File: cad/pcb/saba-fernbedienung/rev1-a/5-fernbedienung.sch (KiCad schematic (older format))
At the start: 49 parts, among them K601 G6K-2, K602 G6K-2, K603 G6K-2, K604 G6K-2, K605 G6K-2, K606 G6K-2, K607 EC2-5TNU, Q601 BC846, Q602 BC846, Q603 BC846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

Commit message: Fix: Div. DRC
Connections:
- no-connect marks 6 -> 12
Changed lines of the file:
@@
 Text Notes 4100 5150 0    79   ~ 0
 Netzschalter
+NoConn ~ 7650 2800
+NoConn ~ 7850 2800
+NoConn ~ 7650 4200
+NoConn ~ 7850 4200
+NoConn ~ 7650 1200
+NoConn ~ 7850 1200
 $EndSCHEMATC

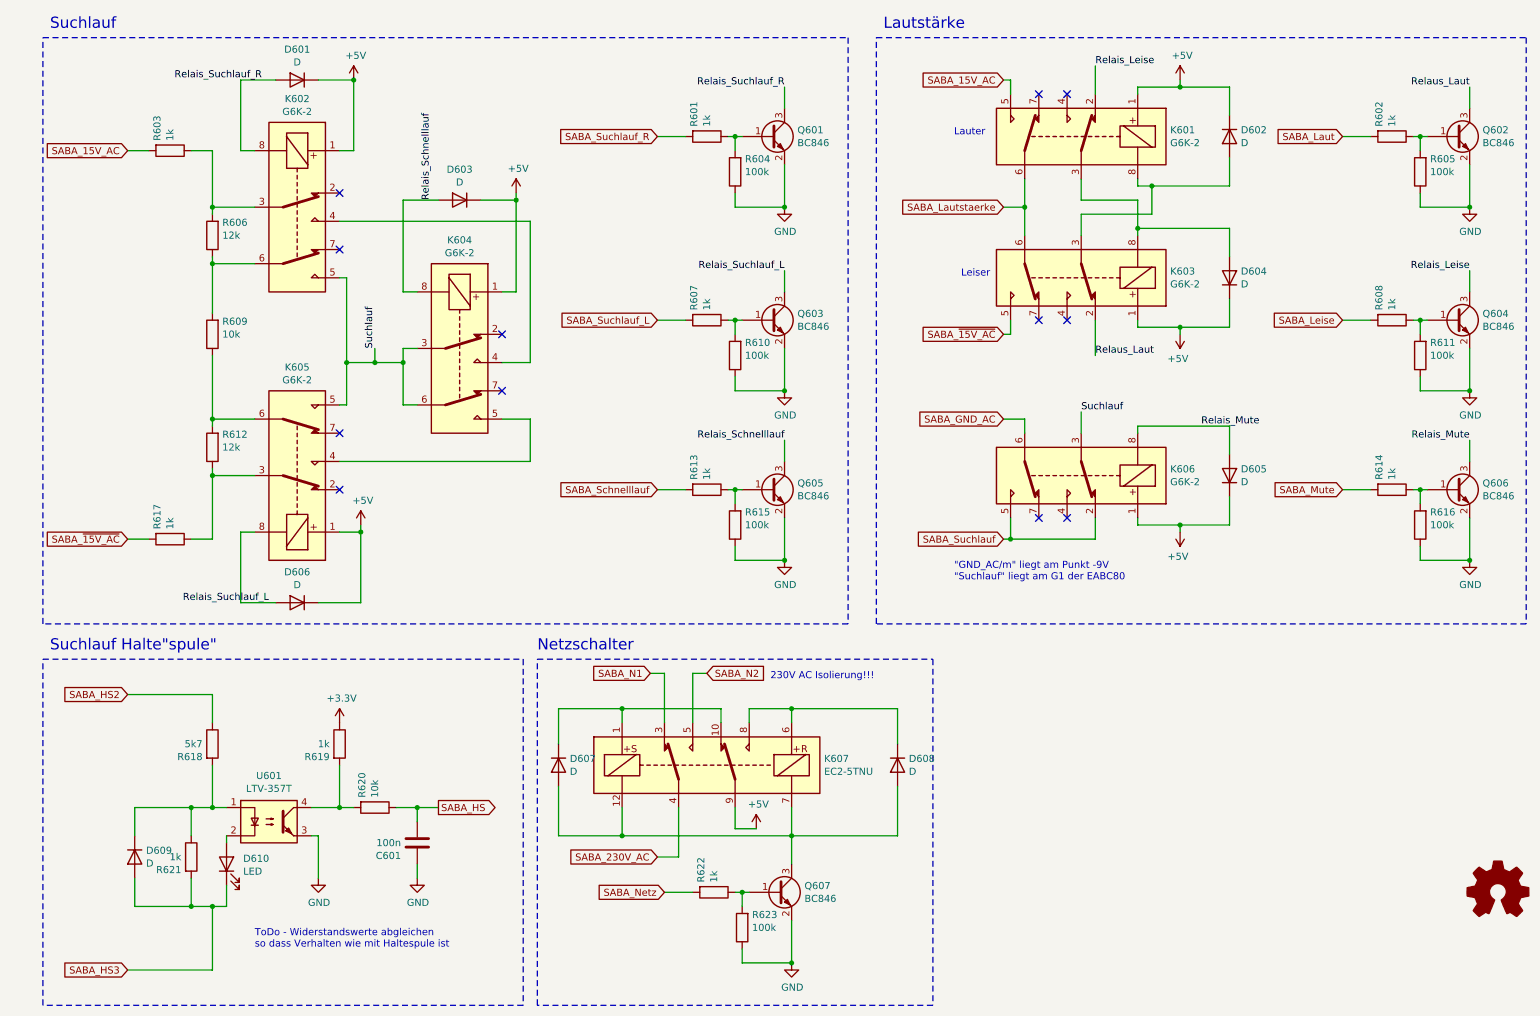
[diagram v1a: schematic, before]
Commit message: New: Bauteil - Pad Zuordnungen
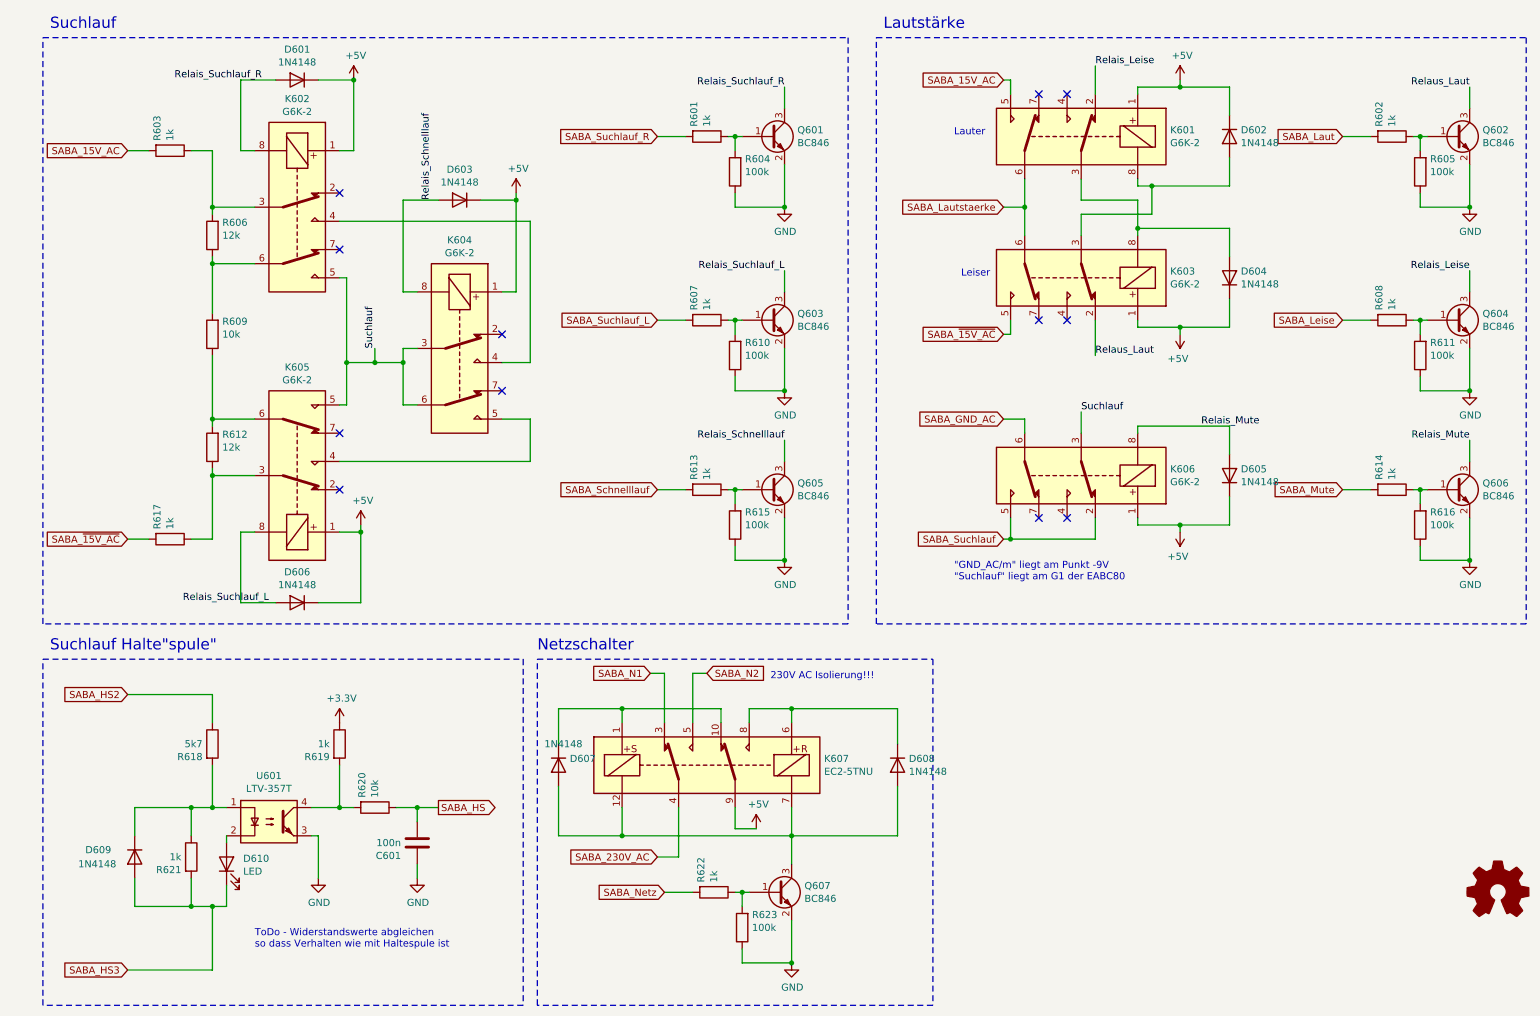
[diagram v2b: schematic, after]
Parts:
- D601, D602, D603, D604, D605, D606, D607, D608, D609: value D -> 1N4148; footprint (none) -> Diode_SMD:D_SOD-323F
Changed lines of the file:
@@
-$EndComp
-$Comp
-L Relay:G6K-2 K604
-U 1 1 60038514
-P 3550 3000
-F 0 "K604" V 2783 3000 50  0000 C CNN
-F 1 "G6K-2" V 2874 3000 50  0000 C CNN
-F 2 "Relay_SMD:Relay_DPDT_Omron_G6K-2F" H 3550 3000 50  0001 L CNN
-F 3 "http://omronfs.omron.com/en_US/ecb/products/pdf/en-g6k.pdf" H 3550 3000 50  0001 C CNN
-	1    3550 3000
-	0    1    1    0
 $EndComp
 $Comp
@@
 P 2400 4800
 F 0 "D606" H 2400 5017 50  0000 C CNN
-F 1 "D" H 2400 4926 50  0000 C CNN
-F 2 "" H 2400 4800 50  0001 C CNN
+F 1 "1N4148" H 2400 4926 50  0000 C CNN
+F 2 "Diode_SMD:D_SOD-323F" H 2400 4800 50  0001 C CNN
 F 3 "~" H 2400 4800 50  0001 C CNN
 	1    2400 4800
@@
 P 3550 1950
 F 0 "D603" H 3550 2167 50  0000 C CNN
-F 1 "D" H 3550 2076 50  0000 C CNN
-F 2 "" H 3550 1950 50  0001 C CNN
+F 1 "1N4148" H 3550 2076 50  0000 C CNN
+F 2 "Diode_SMD:D_SOD-323F" H 3550 1950 50  0001 C CNN
 F 3 "~" H 3550 1950 50  0001 C CNN
 	1    3550 1950
@@
 P 2400 1100
 F 0 "D601" H 2400 1317 50  0000 C CNN
-F 1 "D" H 2400 1226 50  0000 C CNN
-F 2 "" H 2400 1100 50  0001 C CNN
+F 1 "1N4148" H 2400 1226 50  0000 C CNN
+F 2 "Diode_SMD:D_SOD-323F" H 2400 1100 50  0001 C CNN
 F 3 "~" H 2400 1100 50  0001 C CNN
 	1    2400 1100
@@
 Connection ~ 2750 3100
 Wire Wire Line
-	3150 3400 3150 3100
-Wire Wire Line
 	2750 3100 2750 3400
-Wire Wire Line
-	3950 2600 3950 1950
 Wire Wire Line
 	3150 1950 3400 1950
@@
 Relais_Suchlauf_L
 Wire Wire Line
-	3250 3400 3150 3400
-Wire Wire Line
-	3250 3000 3150 3000
-Wire Wire Line
-	3150 3000 3150 3100
-Connection ~ 3150 3100
-Wire Wire Line
-	4050 3100 3850 3100
-Wire Wire Line
 	4050 2100 4050 3100
-Wire Wire Line
-	4050 3500 3850 3500
-Wire Wire Line
-	3950 2600 3850 2600
-Wire Wire Line
-	3250 2600 3150 2600
 Text GLabel 4950 4000 0    50   Input ~ 0
 SABA_Schnelllauf
@@
 	1    0    0    -1
 $EndComp
-Wire Wire Line
-	3150 1950 3150 2600
 Wire Wire Line
 	2000 1100 2000 1600
@@
 U 1 1 6014EEE0
 P 1250 6600
-F 0 "D609" V 1204 6520 50  0000 R CNN
-F 1 "D" V 1295 6520 50  0000 R CNN
-F 2 "" H 1250 6600 50  0001 C CNN
+F 0 "D609" V 1200 6950 50  0000 R CNN
+F 1 "1N4148" V 1300 7000 50  0000 R CNN
+F 2 "Diode_SMD:D_SOD-323F" H 1250 6600 50  0001 C CNN
 F 3 "~" H 1250 6600 50  0001 C CNN
 	1    1250 6600
@@
 NoConn ~ 2700 1900
 NoConn ~ 2700 2300
-NoConn ~ 3850 2900
-NoConn ~ 3850 3300
 NoConn ~ 2700 3600
 NoConn ~ 2700 4000
@@
 P 9000 1500
 F 0 "D602" V 8954 1420 50  0000 R CNN
-F 1 "D" V 9045 1420 50  0000 R CNN
-F 2 "" H 9000 1500 50  0001 C CNN
+F 1 "1N4148" V 9045 1420 50  0000 R CNN
+F 2 "Diode_SMD:D_SOD-323F" H 9000 1500 50  0001 C CNN
 F 3 "~" H 9000 1500 50  0001 C CNN
 	1    9000 1500
@@
 P 9000 2500
 F 0 "D604" V 9046 2580 50  0000 L CNN
-F 1 "D" V 8955 2580 50  0000 L CNN
-F 2 "" H 9000 2500 50  0001 C CNN
+F 1 "1N4148" V 8955 2580 50  0000 L CNN
+F 2 "Diode_SMD:D_SOD-323F" H 9000 2500 50  0001 C CNN
 F 3 "~" H 9000 2500 50  0001 C CNN
 	1    9000 2500
@@
 P 9000 3900
 F 0 "D605" V 9046 3980 50  0000 L CNN
-F 1 "D" V 8955 3980 50  0000 L CNN
-F 2 "" H 9000 3900 50  0001 C CNN
+F 1 "1N4148" V 8955 3980 50  0000 L CNN
+F 2 "Diode_SMD:D_SOD-323F" H 9000 3900 50  0001 C CNN
 F 3 "~" H 9000 3900 50  0001 C CNN
 	1    9000 3900
@@
 	2950 3000 2950 3100
 Connection ~ 2950 3100
-Wire Wire Line
-	2950 3100 3150 3100
 Text Label 7950 3450 0    50   ~ 0
 Suchlauf
@@
 P 4250 5950
 F 0 "D607" V 4204 5870 50  0000 R CNN
-F 1 "D" V 4295 5870 50  0000 R CNN
-F 2 "" H 4250 5950 50  0001 C CNN
+F 1 "1N4148" V 4100 6050 50  0000 R CNN
+F 2 "Diode_SMD:D_SOD-323F" H 4250 5950 50  0001 C CNN
 F 3 "~" H 4250 5950 50  0001 C CNN
 	1    4250 5950
@@
 P 6650 5950
 F 0 "D608" V 6604 5870 50  0000 R CNN
-F 1 "D" V 6695 5870 50  0000 R CNN
-F 2 "" H 6650 5950 50  0001 C CNN
+F 1 "1N4148" V 6695 5870 50  0000 R CNN
+F 2 "Diode_SMD:D_SOD-323F" H 6650 5950 50  0001 C CNN
 F 3 "~" H 6650 5950 50  0001 C CNN
 	1    6650 5950
@@
 NoConn ~ 7650 1200
 NoConn ~ 7850 1200
+Wire Wire Line
+	2950 3100 3150 3100
+NoConn ~ 3850 3300
+NoConn ~ 3850 2900
+Wire Wire Line
+	3150 1950 3150 2600
+Wire Wire Line
+	3250 2600 3150 2600
+Wire Wire Line
+	3950 2600 3850 2600
+Wire Wire Line
+	4050 3500 3850 3500
+Wire Wire Line
+	4050 3100 3850 3100
+Connection ~ 3150 3100
+Wire Wire Line
+	3150 3000 3150 3100
+Wire Wire Line
+	3250 3000 3150 3000
+Wire Wire Line
+	3250 3400 3150 3400
+Wire Wire Line
+	3950 2600 3950 1950
+Wire Wire Line
+	3150 3400 3150 3100
+$Comp
+L Relay:G6K-2 K604
+U 1 1 60038514
+P 3550 3000
+F 0 "K604" V 2783 3000 50  0000 C CNN
+F 1 "G6K-2" V 2874 3000 50  0000 C CNN
+F 2 "Relay_SMD:Relay_DPDT_Omron_G6K-2F" H 3550 3000 50  0001 L CNN
+F 3 "http://omronfs.omron.com/en_US/ecb/products/pdf/en-g6k.pdf" H 3550 3000 50  0001 C CNN
+	1    3550 3000
+	0    1    1    0
+$EndComp
 $EndSCHEMATC

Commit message: Add: Bauteiltypen Digikey...
viele Bauteile von WE da hoffentlich lange gueltig...
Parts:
- C601: Bauteil (none) -> WE 885382206004
- D601, D602, D603, D604, D605, D606, D607, D608, D609: Bauteil (none) -> ON 1N4148WS
- D610: Bauteil (none) -> WE 150080BS75000
- K601, K602, K603, K604, K605, K606: Bauteil (none) -> Omron G6K-2F-TR DC5
- K607: Bauteil (none) -> Kemet EC2-5TNU
- Q601, Q602, Q603, Q604, Q605, Q606, Q607: Bauteil (none) -> ON BC846BLT3G
- U601: Bauteil (none) -> Lite-On LTV-357T

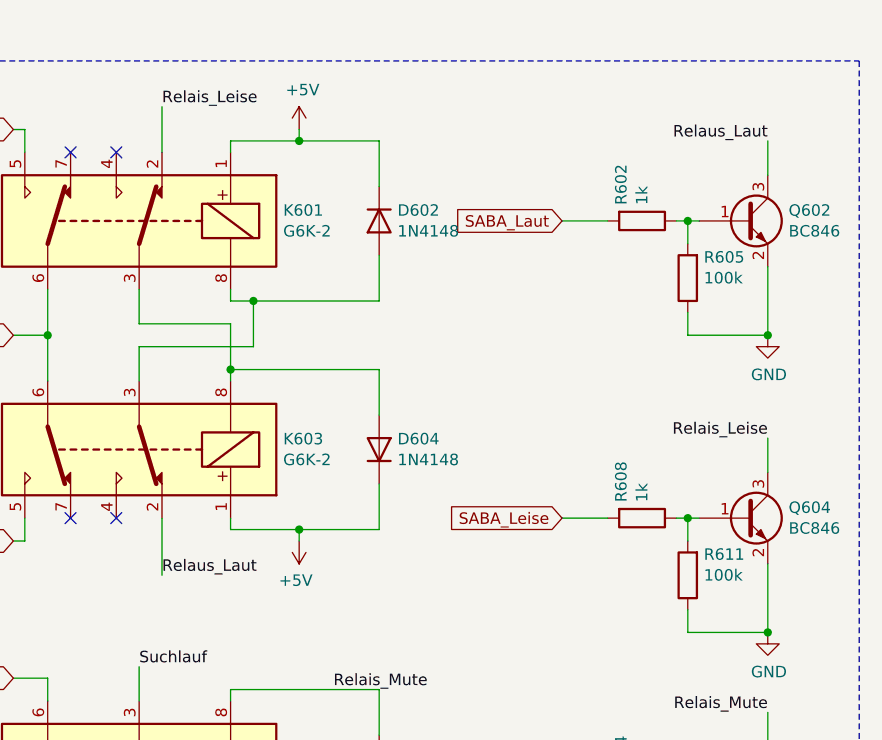
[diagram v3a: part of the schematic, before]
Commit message: Change: Relais SMT -> THT, Sicherung PCB
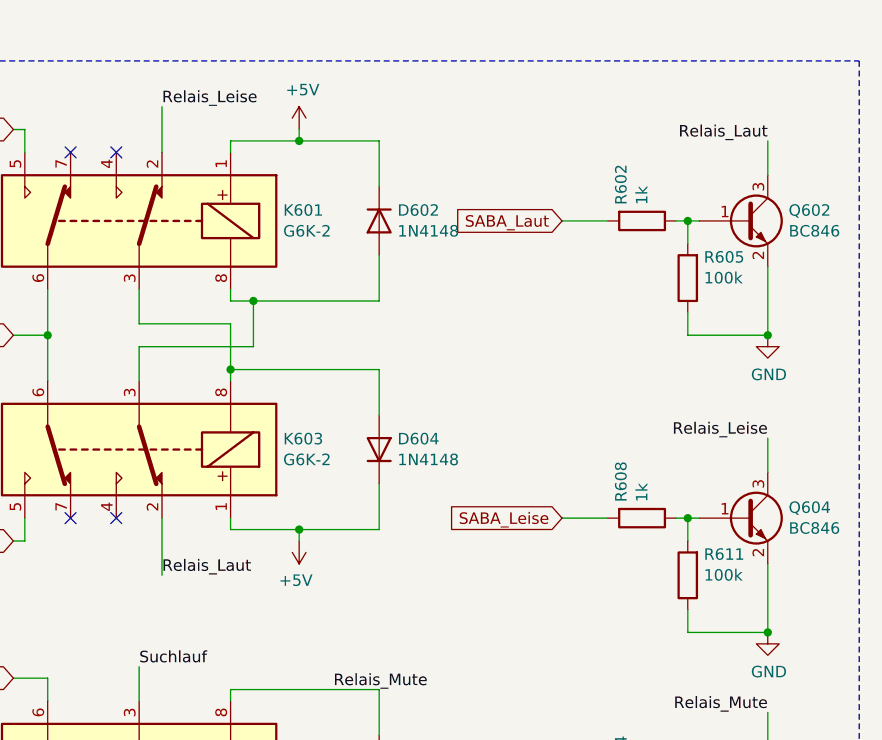
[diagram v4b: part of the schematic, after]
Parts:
- K601, K602, K603, K604, K605, K606: footprint Relay_SMD:Relay_DPDT_Omron_G6K-2F -> Relay_THT:Relay_DPDT_Omron_G6K-2P; Bauteil Omron G6K-2F-TR DC5 -> Omron G6K-2P DC5
- R603, R617: footprint Resistor_SMD:R_0603_1608Metric -> Resistor_THT:R_Axial_DIN0207_L6.3mm_D2.5mm_P7.62mm_Horizontal
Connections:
- net Relaus_Laut renamed Relais_Laut
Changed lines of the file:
@@
 encoding utf-8
 Sheet 6 7
-Title "Fernbedienung SABA 6-3D"
-Date "2021-01-13"
+Title "Fernbedienung - Webradio SABA 6-3D"
+Date "2021-01-14"
 Rev "1-A"
 Comp "Martin Wagner DL2WAG"
@@
 Comment2 "Fernbedienung"
 Comment3 "(Meersburg/Freiburg 6-3D, weitere?)"
-Comment4 "Fernbedienung für SABA \"Automatic\" Radios"
+Comment4 "Fernbedienung - Webradio für SABA \"Automatic\" Radios"
 $EndDescr
 $Comp
@@
 F 0 "K602" V 1633 2000 50  0000 C CNN
 F 1 "G6K-2" V 1724 2000 50  0000 C CNN
-F 2 "Relay_SMD:Relay_DPDT_Omron_G6K-2F" H 2400 2000 50  0001 L CNN
+F 2 "Relay_THT:Relay_DPDT_Omron_G6K-2P" H 2400 2000 50  0001 L CNN
 F 3 "http://omronfs.omron.com/en_US/ecb/products/pdf/en-g6k.pdf" H 2400 2000 50  0001 C CNN
-F 4 "Omron G6K-2F-TR DC5" V 2400 2000 50  0001 C CNN "Bauteil"
+F 4 "Omron G6K-2P DC5" V 2400 2000 50  0001 C CNN "Bauteil"
 	1    2400 2000
 	0    1    1    0
@@
 F 0 "R603" H 1430 1509 50  0000 R CNN
 F 1 "1k" H 1430 1600 50  0000 R CNN
-F 2 "Resistor_SMD:R_0603_1608Metric" V 1430 1600 50  0001 C CNN
+F 2 "Resistor_THT:R_Axial_DIN0207_L6.3mm_D2.5mm_P7.62mm_Horizontal" V 1430 1600 50  0001 C CNN
 F 3 "~" H 1500 1600 50  0001 C CNN
 F 4 "" V 1500 1650 50  0000 R CNN "Placement"
@@
 F 0 "R617" H 1430 4259 50  0000 R CNN
 F 1 "1k" H 1430 4350 50  0000 R CNN
-F 2 "Resistor_SMD:R_0603_1608Metric" V 1430 4350 50  0001 C CNN
+F 2 "Resistor_THT:R_Axial_DIN0207_L6.3mm_D2.5mm_P7.62mm_Horizontal" V 1430 4350 50  0001 C CNN
 F 3 "~" H 1500 4350 50  0001 C CNN
 F 4 "" V 1500 4400 50  0000 R CNN "Placement"
@@
 $EndComp
 $Comp
-L Device:D D604
-U 1 1 60234C49
-P 9000 2500
-F 0 "D604" V 9046 2580 50  0000 L CNN
-F 1 "1N4148" V 8955 2580 50  0000 L CNN
-F 2 "Diode_SMD:D_SOD-323F" H 9000 2500 50  0001 C CNN
-F 3 "~" H 9000 2500 50  0001 C CNN
-F 4 "ON 1N4148WS" V 9000 2500 50  0001 C CNN "Bauteil"
-	1    9000 2500
-	0    1    -1   0
-$EndComp
-$Comp
 L power:+5V #PWR0602
 U 1 1 60235763
@@
 	8650 2850 8350 2850
 Text Label 8050 3050 0    50   ~ 0
-Relaus_Laut
+Relais_Laut
 Text Label 8050 1000 0    50   ~ 0
 Relais_Leise
 Text Label 10700 1150 2    50   ~ 0
-Relaus_Laut
+Relais_Laut
 Text Label 10700 2450 2    50   ~ 0
 Relais_Leise
@@
 F 0 "K606" H 7320 3854 50  0000 R CNN
 F 1 "G6K-2" H 7320 3945 50  0000 R CNN
-F 2 "Relay_SMD:Relay_DPDT_Omron_G6K-2F" H 7950 3900 50  0001 L CNN
+F 2 "Relay_THT:Relay_DPDT_Omron_G6K-2P" H 7950 3900 50  0001 L CNN
 F 3 "http://omronfs.omron.com/en_US/ecb/products/pdf/en-g6k.pdf" H 7950 3900 50  0001 C CNN
-F 4 "Omron G6K-2F-TR DC5" H 7950 3900 50  0001 C CNN "Bauteil"
+F 4 "Omron G6K-2P DC5" H 7950 3900 50  0001 C CNN "Bauteil"
 	1    7950 3900
 	-1   0    0    1
@@
 F 0 "K603" H 7320 2454 50  0000 R CNN
 F 1 "G6K-2" H 7320 2545 50  0000 R CNN
-F 2 "Relay_SMD:Relay_DPDT_Omron_G6K-2F" H 7950 2500 50  0001 L CNN
+F 2 "Relay_THT:Relay_DPDT_Omron_G6K-2P" H 7950 2500 50  0001 L CNN
 F 3 "http://omronfs.omron.com/en_US/ecb/products/pdf/en-g6k.pdf" H 7950 2500 50  0001 C CNN
-F 4 "Omron G6K-2F-TR DC5" H 7950 2500 50  0001 C CNN "Bauteil"
+F 4 "Omron G6K-2P DC5" H 7950 2500 50  0001 C CNN "Bauteil"
 	1    7950 2500
 	-1   0    0    1
@@
 F 0 "K601" H 7320 1546 50  0000 R CNN
 F 1 "G6K-2" H 7320 1455 50  0000 R CNN
-F 2 "Relay_SMD:Relay_DPDT_Omron_G6K-2F" H 7950 1500 50  0001 L CNN
+F 2 "Relay_THT:Relay_DPDT_Omron_G6K-2P" H 7950 1500 50  0001 L CNN
 F 3 "http://omronfs.omron.com/en_US/ecb/products/pdf/en-g6k.pdf" H 7950 1500 50  0001 C CNN
-F 4 "Omron G6K-2F-TR DC5" H 7950 1500 50  0001 C CNN "Bauteil"
+F 4 "Omron G6K-2P DC5" H 7950 1500 50  0001 C CNN "Bauteil"
 	1    7950 1500
 	-1   0    0    -1
@@
 F 0 "K605" V 3167 3900 50  0000 C CNN
 F 1 "G6K-2" V 3076 3900 50  0000 C CNN
-F 2 "Relay_SMD:Relay_DPDT_Omron_G6K-2F" H 2400 3900 50  0001 L CNN
+F 2 "Relay_THT:Relay_DPDT_Omron_G6K-2P" H 2400 3900 50  0001 L CNN
 F 3 "http://omronfs.omron.com/en_US/ecb/products/pdf/en-g6k.pdf" H 2400 3900 50  0001 C CNN
-F 4 "Omron G6K-2F-TR DC5" V 2400 3900 50  0001 C CNN "Bauteil"
+F 4 "Omron G6K-2P DC5" V 2400 3900 50  0001 C CNN "Bauteil"
 	1    2400 3900
 	0    1    -1   0
@@
 F 0 "K604" V 2783 3000 50  0000 C CNN
 F 1 "G6K-2" V 2874 3000 50  0000 C CNN
-F 2 "Relay_SMD:Relay_DPDT_Omron_G6K-2F" H 3550 3000 50  0001 L CNN
+F 2 "Relay_THT:Relay_DPDT_Omron_G6K-2P" H 3550 3000 50  0001 L CNN
 F 3 "http://omronfs.omron.com/en_US/ecb/products/pdf/en-g6k.pdf" H 3550 3000 50  0001 C CNN
-F 4 "Omron G6K-2F-TR DC5" V 3550 3000 50  0001 C CNN "Bauteil"
+F 4 "Omron G6K-2P DC5" V 3550 3000 50  0001 C CNN "Bauteil"
 	1    3550 3000
 	0    1    1    0
 $EndComp
+$Comp
+L Device:D D604
+U 1 1 60234C49
+P 9000 2500
+F 0 "D604" V 9046 2580 50  0000 L CNN
+F 1 "1N4148" V 8955 2580 50  0000 L CNN
+F 2 "Diode_SMD:D_SOD-323F" H 9000 2500 50  0001 C CNN
+F 3 "~" H 9000 2500 50  0001 C CNN
+F 4 "ON 1N4148WS" V 9000 2500 50  0001 C CNN "Bauteil"
+	1    9000 2500
+	0    1    -1   0
+$EndComp
 $EndSCHEMATC
